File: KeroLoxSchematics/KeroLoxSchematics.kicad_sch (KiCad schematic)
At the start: 9 parts

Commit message: GSE -> Rocket Schem finished
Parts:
- added J1: Ignitor1_Output, symbol Connector:Screw_Terminal_01x02
- added J2: Ignitor2_Output, symbol Connector:Screw_Terminal_01x02
- added M1: LOX_Injector, symbol Motor:Motor_Servo
- added M2: LOX_Dump, symbol Motor:Motor_Servo
- added M3: LOX_Vent_Valve, symbol Motor:Motor_Servo
- added M4: Kero_Vent_Valve, symbol Motor:Motor_Servo
- added R1: LOX Pressurizing Valve, symbol Device:R
- added R10, R11, R12, R8, R9: 250 OHM, symbol Device:R
- added R2: GN2 Pressurizing Valve, symbol Device:R
- added R5: Kero_Injector_Valve, symbol Device:R
- added R6, R7: 1 OHM 2W, symbol Device:R
- added U10: Kero_Tank, symbol KeroLoxPT:PressureTransducer
- added U11: LOX_Inj_Line, symbol KeroLoxPT:PressureTransducer
- added U12: Kero_Inj_Line, symbol KeroLoxPT:PressureTransducer
- added U13: Combusion_Chamber, symbol KeroLoxPT:PressureTransducer
- added U14, U15: HX711, symbol KeroLoxLoadcell:HX711
- added U16: Thurst_Load_Cell, symbol KeroLoxLoadcell:LoadCell
- added U17: Rocket_Weight_Load_Cell, symbol KeroLoxLoadcell:LoadCell
- added U18: ~, symbol KeroLox_SDCard:SD_Card
- added U6: ~, symbol KeroLoxRelay:RelayBlock
- added U7, U8: LM338_TO220, Package_TO_SOT_THT:TO-220-3_Vertical, symbol Regulator_Linear:LM337_TO220
- added U9: LOX_Tank, symbol KeroLoxPT:PressureTransducer
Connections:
- net Earth: now also U16.9 (SHIELD)
- net GSE_ROCKET_29.6V: now reaches BT3.1 (+), U3. (GND), U4.1 (Vin), U5.1 (Vin)
- net at BT2.2 (-), U2.0 (GND), U3.0 (GND): now also U14.5 (GND), U15.5 (GND)
- net GSE_BATTERY_24V: now reaches BT1.1 (+), U2.1 (Vin), U3.1 (Vin)
- net ROCKET_12.6V: now reaches A1.30 (VIN), U5. (GND)
- net ROCKET_12.6V: now also M1.2 (+), M2.2 (+), M3.2 (+), M4.2 (+)
- net at A1.4 (GND), U5. (GND): now also U4. (GND), J1.2 (Pin_2), J2.2 (Pin_2), M1.3 (-), M2.3 (-), M3.3 (-), M4.3 (-), R1.2, R10.2, R11.2, R12.2, R2.2, R5.2, R8.2, R9.2, U18.4 (GND), U6. (NO8)
- net GSE_5V: now reaches U1.0 (GPIO25), U2. (GND)
- net GSE_5V: now also A1. (USB), U1.1 (5V), U1.2 (USB), U14.1 (VCC), U14.16 (VDD), U15.1 (VCC), U15.16 (VDD)
- net at A1.10 (D7): now also U6. (NO8)
- net at A1.11 (D8): now also U6. (NO8)
- net at A1.12 (D9): now also U6. (NO8)
- net at A1.14 (D11): now also U18.8 (DAT1)
- net at A1.15 (D12): now also U18.7 (DAT0)
- net at A1.16 (D13): now also U18.5 (CLK)
- net at A1.19 (A0): now also R8.1, U9.2 (-)
- net at A1.20 (A1): now also R9.1, U10.2 (-)
- net at A1.21 (A2): now also R10.1, U11.2 (-)
- net at A1.22 (A3): now also R11.1, U12.2 (-)
- net at A1.23 (A4): now also R12.1, U13.2 (-)
- net at A1.27 (+5V): now also U18.3 (CS), U18.6 (5V)
- net at A1.5 (D2): now also M1.1 (PWM)
- net at A1.6 (D3): now also M2.1 (PWM)
- net at A1.7 (D4): now also M3.1 (PWM)
- net at A1.8 (D5): now also M4.1 (PWM)
- net at A1.9 (D6): now also U6. (NO8)
- net ROCKET_24V: now reaches U4. (GND)
- net ROCKET_24V: now also U10.1 (+), U11.1 (+), U12.1 (+), U13.1 (+), U6. (NO8), U9.1 (+)
- new net: J1.1 (Pin_1), R6.2, U7.1 (ADJ)
- new net: U6. (NO8), U7.2 (VI)
- new net: R6.1, U7.3 (VO)
- new net: U15.10 (INE+), U17.10 (INE+)
- new net: U15.7 (INA-), U17.7 (INA-)
- new net: U15.8 (INA+), U17.8 (INA+)
- new net: U15.9 (SHIELD), U17.9 (SHIELD)
- new net: U14.10 (INE+), U16.10 (INE+)
- new net: U1.0 (GPIO25), U14.11 (SCK)
- new net: U1.0 (GPIO25), U14.12 (DAT)
- new net: U14.7 (INA-), U16.7 (INA-)
- new net: U14.8 (INA+), U16.8 (INA+)
- new net: U14.9 (SHIELD), U16.9 (SHIELD)
- new net: U1.0 (GPIO25), U15.11 (SCK)
- new net: U1.0 (GPIO25), U15.12 (DAT)
- new net: J2.1 (Pin_1), R7.2, U8.1 (ADJ)
- new net: U6. (NO8), U8.2 (VI)
- new net: R7.1, U8.3 (VO)
- new net: R5.1, U6. (NO8)
- new net: R1.1, R2.1, U6. (NO8)
- new net GSE Box Chassis: U17.9 (SHIELD)
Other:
- note added: "12.6V Regulator"
- note added: "24V Buck Regulator"
- note added: "29.6V Boost Regulator"
- note added: "5V 3A Buck Regulator"
- note added: "8 Relay Board 24v Coils"
- note added: "Ground System Electronics (GSE)"
- note added: "Ignitor Control Unit (ICU)"
- note added: "Rocket Onboard ELectronics"
- note added: "SD CARD FOR FLIGHT CONFIG ONLY"
- note added: "Transducer Current Converter (TCC)"
- note removed: "12V Regulator"
- note removed: "24V Regulator"
- note removed: "5V 3A Regulator"
- note removed: "Ground System Electronics"
- moved on the sheet: BT1, BT2, BT3, U4, U5

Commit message: Finalized Schematic
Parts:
- added BT4: 24V_Battery, symbol Device:Battery
- added U19: MikroTek HEX, symbol KeroLox_Ethernet:MikroTek_HEX
- added U20, U23: POE Injector, symbol KeroLox_Ethernet:POE_Injector
- added U21, U22: Ubiquiti NanoBeam, symbol KeroLox_Ethernet:Ubiquiti_NanoBeam
- added U24: Ian's Laptop, symbol KeroLox_Ethernet:Ians_Laptop
- BT1, BT2: value Battery -> 12V_Battery
- BT3: value Battery -> 29.6V_Battery
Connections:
- net GSE_5V: no longer A1. (USB), U1.2 (USB)
- net GSE_BATTERY_24V: now also U19. (Ethernet4), U20. (POE_OUT)
- net at BT2.2 (-), U14.5 (GND), U15.5 (GND)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: now also U19. (Ethernet4), U20. (POE_OUT)
- net at U15.9 (SHIELD): no longer U17.9 (SHIELD)
- net at U14.9 (SHIELD): now also U16.9 (SHIELD)
- net Earthed on Rocket Chassis: now reaches U16.9 (SHIELD)
- net Earthed on Rocket Chassis: now also BT3.2 (-), U3. (GND), U4.0 (GND), U5.0 (GND); no longer U14.9 (SHIELD)
- net at U1.3 (Ethernet): now also U19. (Ethernet4)
- removed net Earth: BT3.2 (-), U16.9 (SHIELD), U3. (GND), U4.0 (GND), U5.0 (GND)
- new net: U15.9 (SHIELD), U17.9 (SHIELD)
- new net: A1. (USB), U1.2 (USB)
- new net: BT4.1 (+), U23. (POE_OUT)
- new net: BT4.2 (-), U23. (POE_OUT)
- new net: U20. (POE_OUT), U21. (LAN_IN)
- new net: U23. (POE_OUT), U24. (Ethernet)
- new net: U19. (Ethernet4), U20. (POE_OUT)
- new net: U22. (LAN_IN), U23. (POE_OUT)
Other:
- note added: "Access Point"
- note removed: "29.6V Battery"
- note removed: "2x 12v Batteries"
- company: (none) -> Mines Deflagration Research Lab
- title: (none) -> KeroLox Full Schematic
- moved on the sheet: A1, BT1, BT2, BT3, J1, J2, M1, M2, M3, M4, R1, R10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

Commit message: Cosmetic Changes
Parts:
- U10: value Kero_Tank -> Kero_Tank_PT
- U11: value LOX_Inj_Line -> LOX_Inj_Line_PT
- U12: value Kero_Inj_Line -> Kero_Inj_Line_PT
- U13: value Combusion_Chamber -> Combusion_Chamber_PT
- U9: value LOX_Tank -> LOX_Tank_PT
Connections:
- net at U15.9 (SHIELD): no longer U17.9 (SHIELD)
- net at U14.9 (SHIELD): now also U16.9 (SHIELD)
- new net: U15.9 (SHIELD), U17.9 (SHIELD)
- new net: U19. (Ethernet4), U20. (POE_OUT)
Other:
- moved on the sheet: J1, J2

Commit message: Changed PT grounding arcitecture
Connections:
- net at U15.9 (SHIELD): no longer U17.9 (SHIELD)
- net at A1.4 (GND), J1.2 (Pin_2), J2.2 (Pin_2)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: no longer R10.2, R11.2, R12.2, R8.2, R9.2
- net at U14.9 (SHIELD): now also U16.9 (SHIELD)
- net at A1.29 (GND): now also R10.2, R11.2, R12.2, R8.2, R9.2
- new net: U15.9 (SHIELD), U17.9 (SHIELD)
- new net: U19. (Ethernet4), U20. (POE_OUT)
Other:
- note added: "1"
- note added: "1:"
- note added: "AS SHORT AS POSSIBLE WIRE LENGTH INDEPENDENT GROUND ON ARDUINO"
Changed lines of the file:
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@@
 	)
 	(rectangle
+		(start 406.4 397.51)
+		(end 449.58 403.86)
+		(stroke
+			(width 0)
+			(type default)
+		)
+		(fill
+			(type none)
+		)
+	)
+	(circle
+		(center 378.46 210.82)
+		(radius 2.8398)
+		(stroke
+			(width 0)
+			(type default)
+		)
+		(fill
+			(type none)
+		)
+	)
+	(rectangle
 		(start 62.23 86.36)
 		(end 224.79 241.3)
@@
 		)
 	)
+	(text "1"
+		(exclude_from_sim no)
+		(at 378.714 211.328 0)
+		(effects
+			(font
+				(size 1.905 1.905)
+			)
+		)
+	)
 	(text "SD CARD FOR FLIGHT CONFIG ONLY"
 		(exclude_from_sim no)
@@
 		)
 	)
+	(text "1:\n"
+		(exclude_from_sim no)
+		(at 408.178 401.066 0)
+		(effects
+			(font
+				(size 1.905 1.905)
+			)
+		)
+	)
+	(text "AS SHORT AS POSSIBLE WIRE LENGTH\nINDEPENDENT GROUND ON ARDUINO"
+		(exclude_from_sim no)
+		(at 429.768 401.066 0)
+		(effects
+			(font
+				(size 1.27 1.27)
+			)
+		)
+	)
 	(text "Rocket Onboard ELectronics"
 		(exclude_from_sim no)
@@
 	)
 	(junction
-		(at 403.86 214.63)
+		(at 393.7 257.81)
 		(diameter 0)
 		(color 0 0 0 1)
@@
 	)
 	(junction
-		(at 403.86 247.65)
-		(diameter 0)
-		(color 0 0 0 1)
-	)
-	(junction
 		(at 469.9 102.87)
 		(diameter 0)
@@
 	)
 	(junction
+		(at 393.7 238.76)
+		(diameter 0)
+		(color 0 0 0 1)
+	)
+	(junction
 		(at 336.55 238.76)
 		(diameter 0)
@@
 	)
 	(junction
-		(at 403.86 267.97)
+		(at 393.7 247.65)
 		(diameter 0)
 		(color 0 0 0 1)
@@
 	)
 	(junction
+		(at 393.7 267.97)
+		(diameter 0)
+		(color 0 0 0 1)
+	)
+	(junction
 		(at 375.92 278.13)
 		(diameter 0)
@@
 	)
 	(junction
-		(at 403.86 238.76)
-		(diameter 0)
-		(color 0 0 0 1)
-	)
-	(junction
 		(at 368.3 247.65)
 		(diameter 0)
@@
 	)
 	(junction
-		(at 403.86 257.81)
-		(diameter 0)
-		(color 0 0 0 1)
-	)
-	(junction
 		(at 148.59 101.6)
 		(diameter 0)
@@
 	(wire
 		(pts
+			(xy 393.7 238.76) (xy 391.16 238.76)
+		)
+		(stroke
+			(width 0)
+			(type default)
+			(color 0 0 0 1)
+		)
+	)
+	(wire
+		(pts
 			(xy 373.38 267.97) (xy 373.38 219.71)
 		)
@@
 	(wire
 		(pts
+			(xy 393.7 267.97) (xy 393.7 257.81)
+		)
+		(stroke
+			(width 0)
+			(type default)
+			(color 0 0 0 1)
+		)
+	)
+	(wire
+		(pts
+			(xy 393.7 220.98) (xy 381 220.98)
+		)
+		(stroke
+			(width 0)
+			(type default)
+			(color 0 0 0 1)
+		)
+	)
+	(wire
+		(pts
 			(xy 336.55 186.69) (xy 353.06 186.69)
 		)
@@
 	(wire
 		(pts
+			(xy 393.7 267.97) (xy 391.16 267.97)
+		)
+		(stroke
+			(width 0)
+			(type default)
+			(color 0 0 0 1)
+		)
+	)
+	(wire
+		(pts
 			(xy 398.78 229.87) (xy 421.64 229.87)
 		)
@@
 	(wire
 		(pts
-			(xy 99.06 133.35) (xy 99.06 124.46)
+			(xy 393.7 247.65) (xy 391.16 247.65)
 		)
 		(stroke
 			(width 0)
 			(type default)
-			(color 255 0 255 1)
+			(color 0 0 0 1)
 		)
 	)
 	(wire
 		(pts
-			(xy 214.63 179.07) (xy 226.06 179.07)
+			(xy 99.06 133.35) (xy 99.06 124.46)
 		)
 		(stroke
 			(width 0)
 			(type default)
-			(color 255 0 0 1)
+			(color 255 0 255 1)
 		)
 	)
 	(wire
 		(pts
-			(xy 184.15 219.71) (xy 184.15 151.13)
+			(xy 214.63 179.07) (xy 226.06 179.07)
 		)
 		(stroke
 			(width 0)
 			(type default)
+			(color 255 0 0 1)
 		)
 	)
 	(wire
 		(pts
-			(xy 416.56 180.34) (xy 416.56 262.89)
+			(xy 184.15 219.71) (xy 184.15 151.13)
 		)
 		(stroke
@@
 	(wire
 		(pts
-			(xy 403.86 214.63) (xy 403.86 238.76)
+			(xy 416.56 180.34) (xy 416.56 262.89)
 		)
 		(stroke
 			(width 0)
 			(type default)
-			(color 0 0 0 1)
 		)
 	)
 	(wire
 		(pts
-			(xy 403.86 214.63) (xy 422.91 214.63)
+			(xy 383.54 214.63) (xy 422.91 214.63)
 		)
 		(stroke
@@
 	(wire
 		(pts
+			(xy 393.7 247.65) (xy 393.7 238.76)
+		)
+		(stroke
+			(width 0)
+			(type default)
+			(color 0 0 0 1)
+		)
+	)
+	(wire
+		(pts
 			(xy 386.08 139.7) (xy 358.14 139.7)
 		)
@@
 	(wire
 		(pts
+			(xy 393.7 278.13) (xy 393.7 267.97)
+		)
+		(stroke
+			(width 0)
+			(type default)
+			(color 0 0 0 1)
+		)
+	)
+	(wire
+		(pts
 			(xy 457.2 102.87) (xy 469.9 102.87)
 		)
@@
 	(wire
 		(pts
-			(xy 403.86 247.65) (xy 403.86 257.81)
-		)
-		(stroke
-			(width 0)
-			(type default)
-			(color 0 0 0 1)
-		)
-	)
-	(wire
-		(pts
-			(xy 391.16 247.65) (xy 403.86 247.65)
-		)
-		(stroke
-			(width 0)
-			(type default)
-			(color 0 0 0 1)
-		)
-	)
-	(wire
-		(pts
 			(xy 173.99 118.11) (xy 173.99 157.48)
 		)
@@
 	(wire
 		(pts
-			(xy 403.86 278.13) (xy 391.16 278.13)
+			(xy 393.7 257.81) (xy 391.16 257.81)
 		)
 		(stroke
@@
 	(wire
 		(pts
-			(xy 403.86 267.97) (xy 403.86 278.13)
+			(xy 393.7 238.76) (xy 393.7 220.98)
 		)
 		(stroke
@@
 	(wire
 		(pts
-			(xy 391.16 267.97) (xy 403.86 267.97)
+			(xy 500.38 194.31) (xy 520.7 194.31)
 		)
 		(stroke
 			(width 0)
 			(type default)
-			(color 0 0 0 1)
+			(color 255 0 0 1)
 		)
 	)
 	(wire
 		(pts
-			(xy 500.38 194.31) (xy 520.7 194.31)
+			(xy 391.16 278.13) (xy 393.7 278.13)
 		)
 		(stroke
 			(width 0)
 			(type default)
-			(color 255 0 0 1)
+			(color 0 0 0 1)
 		)
 	)
@@
 	(wire
 		(pts
-			(xy 391.16 238.76) (xy 403.86 238.76)
-		)
-		(stroke
-			(width 0)
-			(type default)
-			(color 0 0 0 1)
-		)
-	)
-	(wire
-		(pts
 			(xy 364.49 217.17) (xy 364.49 177.8)
 		)
@@
 	(wire
 		(pts
-			(xy 383.54 214.63) (xy 403.86 214.63)
-		)
-		(stroke
-			(width 0)
-			(type default)
-			(color 0 0 0 1)
-		)
-	)
-	(wire
-		(pts
 			(xy 422.91 214.63) (xy 422.91 219.71)
 		)
@@
 	(wire
 		(pts
-			(xy 403.86 238.76) (xy 403.86 247.65)
-		)
-		(stroke
-			(width 0)
-			(type default)
-			(color 0 0 0 1)
-		)
-	)
-	(wire
-		(pts
 			(xy 176.53 172.72) (xy 176.53 214.63)
 		)
@@
 	(wire
 		(pts
-			(xy 403.86 257.81) (xy 403.86 267.97)
-		)
-		(stroke
-			(width 0)
-			(type default)
-			(color 0 0 0 1)
-		)
-	)
-	(wire
-		(pts
 			(xy 375.92 278.13) (xy 383.54 278.13)
 		)
@@
 	(wire
 		(pts
+			(xy 393.7 257.81) (xy 393.7 247.65)
+		)
+		(stroke
+			(width 0)
+			(type default)
+			(color 0 0 0 1)
+		)
+	)
+	(wire
+		(pts
 			(xy 469.9 137.16) (xy 476.25 137.16)
 		)
@@
 	(wire
 		(pts
-			(xy 391.16 257.81) (xy 403.86 257.81)
-		)
-		(stroke
-			(width 0)
-			(type default)
-			(color 0 0 0 1)
-		)
-	)
-	(wire
-		(pts
 			(xy 179.07 130.81) (xy 182.88 130.81)
 		)
@@
 		)
 	)
+	(wire
+		(pts
+			(xy 381 220.98) (xy 381 193.04)
+		)
+		(stroke
+			(width 0)
+			(type default)
+			(color 0 0 0 1)
+		)
+	)

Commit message: Add config clarifications
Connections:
- net at U15.9 (SHIELD): no longer U17.9 (SHIELD)
- net at U14.9 (SHIELD): now also U16.9 (SHIELD)
- new net: U15.9 (SHIELD), U17.9 (SHIELD)
- new net: U19. (Ethernet4), U20. (POE_OUT)
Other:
- note added: "THRUST FOR TEST CONFIG ONLY"
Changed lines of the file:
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@@
+		)
+	)
+	(text "THRUST FOR TEST CONFIG ONLY"
+		(exclude_from_sim no)
+		(at 240.284 191.77 0)
+		(effects
+			(font
+				(size 1.27 1.27)
+			)
 		)
 	)

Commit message: Tweaks to schem
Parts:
- added R3: 10K OHM, symbol Device:R
- added R4: 1K OHM, symbol Device:R
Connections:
- net GSE_ROCKET_29.6V: now also R3.1
- net ROCKET_12.6V: now also U6. (NO8)
- net at U15.9 (SHIELD): no longer U17.9 (SHIELD)
- net at A1.4 (GND), J1.2 (Pin_2), J2.2 (Pin_2)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: now also R4.2
- net at U14.9 (SHIELD): now also U16.9 (SHIELD)
- net GND: now reaches U16.9 (SHIELD)
- net GND: now also BT3.2 (-), U3. (GND), U4.0 (GND), U5.0 (GND); no longer U14.9 (SHIELD)
- net at A1.24 (A5): now also R3.2, R4.1
- removed net Earthed on Rocket Chassis: BT3.2 (-), U16.9 (SHIELD), U3. (GND), U4.0 (GND), U5.0 (GND)
- new net: U15.9 (SHIELD), U17.9 (SHIELD)
- new net: U19. (Ethernet4), U20. (POE_OUT)
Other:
- note added: "8 Relay Board 24V Coils"
- note added: "Battery Measurement Board (BMB)"
- note added: "Earthed On Rocket Chassis SINGLE POINT GROUND"
- note added: "Ignitor Control Board (ICB)"
- note added: "Transducer Current Converter Board (TCC)"
- note removed: "8 Relay Board 24v Coils"
- note removed: "Ignitor Control Unit (ICU)"
- note removed: "Transducer Current Converter (TCC)"

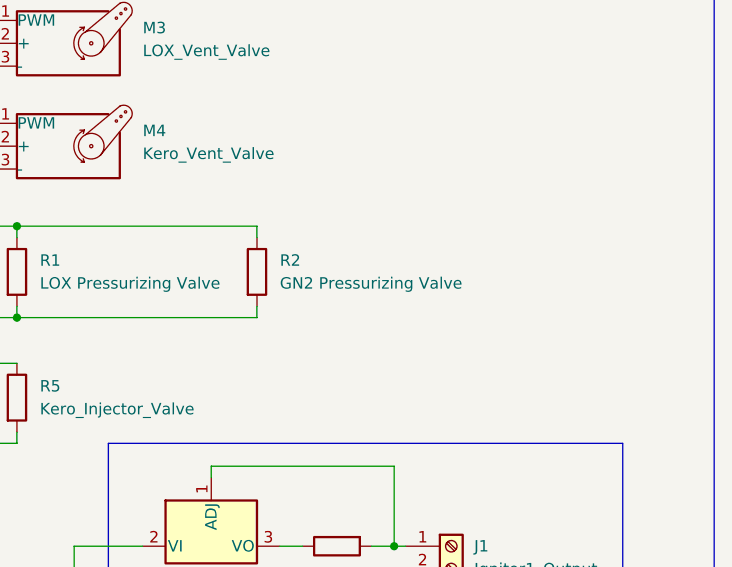
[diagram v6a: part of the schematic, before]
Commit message: Fix Kero Pressure valve naming
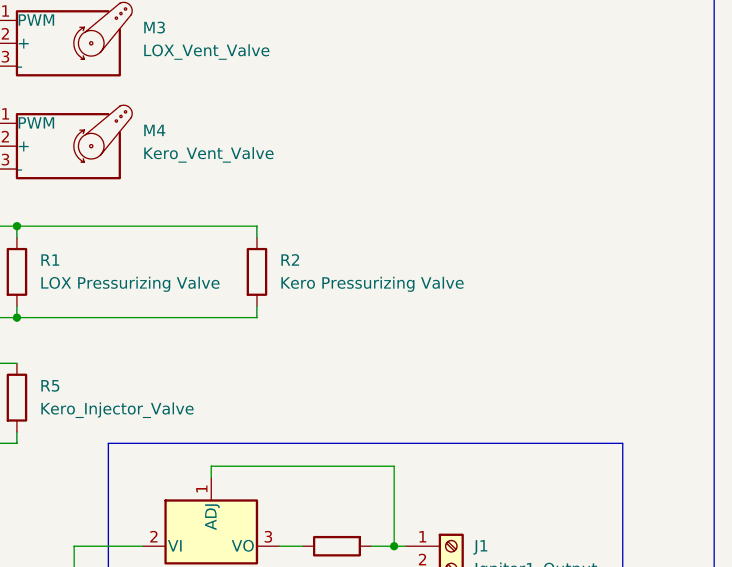
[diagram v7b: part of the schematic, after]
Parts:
- R2: value GN2 Pressurizing Valve -> Kero Pressurizing Valve
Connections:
- net at U15.9 (SHIELD): no longer U17.9 (SHIELD)
- net at U14.9 (SHIELD): now also U16.9 (SHIELD)
- new net: U15.9 (SHIELD), U17.9 (SHIELD)
- new net: U19. (Ethernet4), U20. (POE_OUT)
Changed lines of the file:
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@@
 			)
 		)
-		(property "Value" "GN2 Pressurizing Valve"
+		(property "Value" "Kero Pressurizing Valve"
 			(at 508 152.3999 0)
 			(effects

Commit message: bmb for gse
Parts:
- added R13: 10K OHM, symbol Device:R
- added R14: 1K OHM, symbol Device:R
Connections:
- net GSE_BATTERY_24V: now also R13.1
- net at BT2.2 (-), U14.5 (GND), U15.5 (GND)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: now also R14.2
- net at U15.9 (SHIELD): no longer U17.9 (SHIELD)
- net at U14.9 (SHIELD): now also U16.9 (SHIELD)
- new net: U15.9 (SHIELD), U17.9 (SHIELD)
- new net: R13.2, R14.1, U1.0 (GPIO26)
- new net: U19. (Ethernet4), U20. (POE_OUT)
